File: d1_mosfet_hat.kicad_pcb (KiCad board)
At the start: 2 copper layers, 27.3 x 35.6 mm, 9 parts, among them J1 Pump, J2 Batt, J3 Batt Out, Q1 LL014N, U1 WeMos_mini

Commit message: d1_mosfet shield v1
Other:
- net class Default: clearance 1 -> 0.2
- rule trace_clearance: 1 -> 0.2
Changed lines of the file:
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@@
     (last_trace_width 1)
     (user_trace_width 0.5)
-    (trace_clearance 1)
+    (trace_clearance 0.2)
     (zone_clearance 0.508)
     (zone_45_only no)
@@
     (visible_elements FFFFFF7F)
     (pcbplotparams
-      (layerselection 0x01000_fffffffe)
+      (layerselection 0x010fc_ffffffff)
       (usegerberextensions false)
       (usegerberattributes false)
@@
   (net 6 /GATE)
   (net_class Default "This is the default net class."
-    (clearance 1)
+    (clearance 0.2)
     (trace_width 1)
     (via_dia 0.8)
@@
     (add_net GND)
     (add_net "Net-(D1-Pad1)")
-    (add_net "Net-(U1-Pad1)")
-    (add_net "Net-(U1-Pad10)")
-    (add_net "Net-(U1-Pad11)")
-    (add_net "Net-(U1-Pad12)")
-    (add_net "Net-(U1-Pad13)")
-    (add_net "Net-(U1-Pad14)")
-    (add_net "Net-(U1-Pad15)")
-    (add_net "Net-(U1-Pad16)")
-    (add_net "Net-(U1-Pad3)")
-    (add_net "Net-(U1-Pad4)")
-    (add_net "Net-(U1-Pad5)")
-    (add_net "Net-(U1-Pad7)")
-    (add_net "Net-(U1-Pad8)")
-    (add_net "Net-(U1-Pad9)")
   )
   (module Resistor_SMD:R_0805_2012Metric (layer F.Cu)
@@
   (gr_line (start 151.13 92.71) (end 123.825 92.71) (layer Edge.Cuts) (width 0.15))
   (gr_line (start 151.13 128.27) (end 151.13 92.71) (layer Edge.Cuts) (width 0.15))
-  (via (at 142.24 99.06) (size 0.8) (drill 0.4) (layers F.Cu B.Cu) (net 2))
   (via (at 144.018 107.442) (size 0.8) (drill 0.4) (layers F.Cu B.Cu) (net 1))
   (segment (start 143.905 107.329) (end 144.018 107.442) (width 0.5) (layer F.Cu) (net 1))
@@
   (segment (start 144.975371 115.969629) (end 143.47 117.475) (width 1) (layer B.Cu) (net 1))
   (segment (start 148.911805 115.969629) (end 144.975371 115.969629) (width 1) (layer B.Cu) (net 1))
+  (via (at 142.24 99.06) (size 0.8) (drill 0.4) (layers F.Cu B.Cu) (net 2))
   (via (at 129.54 96.52) (size 0.8) (drill 0.4) (layers F.Cu B.Cu) (net 2))
   (via (at 132.08 96.52) (size 0.8) (drill 0.4) (layers F.Cu B.Cu) (net 2))

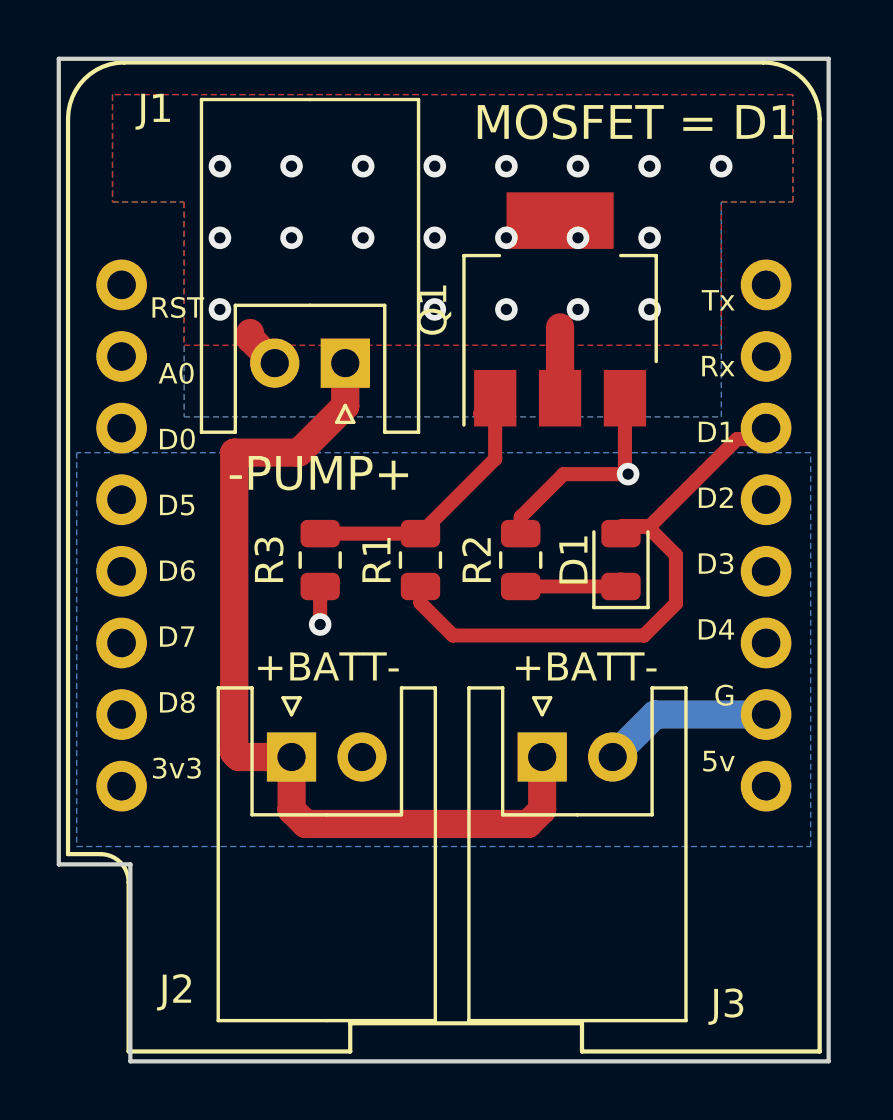
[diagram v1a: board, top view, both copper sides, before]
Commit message: Cat squirter v1.1 - add jumpers to use 5v or 3v power
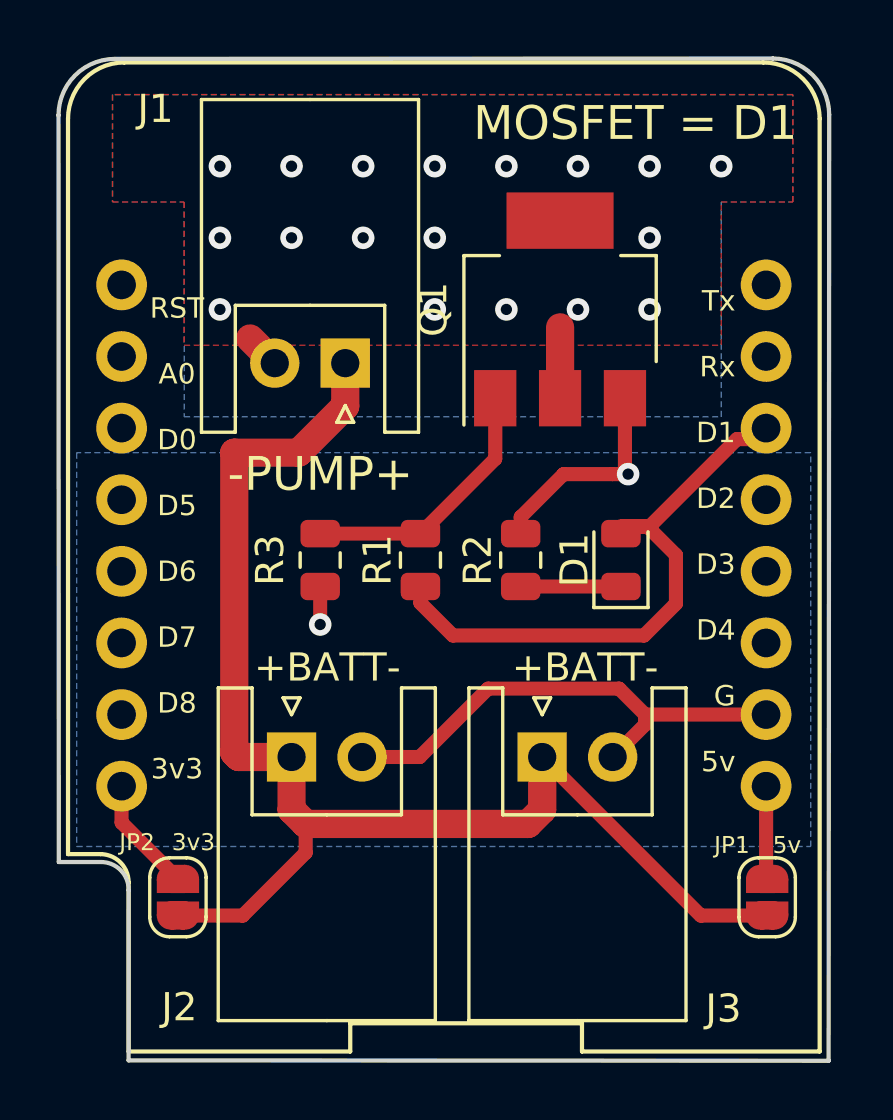
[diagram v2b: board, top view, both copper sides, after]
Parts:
- added JP1: 5v, Jumper:SolderJumper-2_P1.3mm_Open_RoundedPad1.0x1.5mm, F.Cu at (148.9, 122.5)
- added JP2: 3v3, Jumper:SolderJumper-2_P1.3mm_Open_RoundedPad1.0x1.5mm, F.Cu at (128.1, 122.5)
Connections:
- Q1 pad 4: /DRAIN -> (no net)
- U1 pad 1: (no net) -> /5v
- U1 pad 10: (no net) -> unconnected-(U1-Pad10)
- U1 pad 11: (no net) -> unconnected-(U1-Pad11)
- U1 pad 12: (no net) -> unconnected-(U1-Pad12)
- U1 pad 13: (no net) -> unconnected-(U1-Pad13)
- U1 pad 14: (no net) -> unconnected-(U1-Pad14)
- U1 pad 15: (no net) -> unconnected-(U1-Pad15)
- U1 pad 16: (no net) -> /3v3
- U1 pad 3: (no net) -> unconnected-(U1-Pad3)
- U1 pad 4: (no net) -> unconnected-(U1-Pad4)
- U1 pad 5: (no net) -> unconnected-(U1-Pad5)
- U1 pad 7: (no net) -> unconnected-(U1-Pad7)
- U1 pad 8: (no net) -> unconnected-(U1-Pad8)
- U1 pad 9: (no net) -> unconnected-(U1-Pad9)
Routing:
- net /BATT+: track 31.9 -> 48.7 mm
- net GND: track 15.2 -> 26.8 mm
- net /3v3: track 0.00 -> 4.12 mm
- net /5v: track 0.00 -> 3.25 mm
- net /GATE: track 10.2 -> 9.46 mm
- net /D1: track 21.3 -> 20.7 mm
- net /DRAIN: track 3.95 -> 3.75 mm, vias 20 -> 18
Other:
- board size 27.3 x 35.6 mm -> 27.3 x 35.5 mm
- net class Default removed
- board text added: "Battery JP1=open JP2=open 5v pump JP1=close JP2=close 3v pump JP1=open JP2=close Fire JP1=close JP2=close"
- board text added: "accelerando.com.au v1.1 2022-12-03"
- board text removed: "accelerando.com.au 2019-09-14"
